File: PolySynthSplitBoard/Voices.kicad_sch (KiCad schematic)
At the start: 23 parts, among them U701 TCA9548APWR, U702 V1, U703 V4, U704 V2, U705 V5, U706 V3, U707 V6

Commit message: SPI and board tweaks
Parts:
- added R716: LOOP, Resistor_THT:R_Axial_DIN0204_L3.6mm_D1.6mm_P5.08mm_Horizontal, symbol Device:R_US
- added TP701: SCLV1, TestPoint:TestPoint_THTPad_D1.0mm_Drill0.5mm_VAL, symbol Connector:TestPoint
- added TP702: SDAV1, TestPoint:TestPoint_THTPad_D1.0mm_Drill0.5mm_VAL, symbol Connector:TestPoint
- added TP703: SCLV2, TestPoint:TestPoint_THTPad_D1.0mm_Drill0.5mm_VAL, symbol Connector:TestPoint
- added TP704: SDAV2, TestPoint:TestPoint_THTPad_D1.0mm_Drill0.5mm_VAL, symbol Connector:TestPoint
- added TP705: SCLV3, TestPoint:TestPoint_THTPad_D1.0mm_Drill0.5mm_VAL, symbol Connector:TestPoint
- added TP706: SDAV3, TestPoint:TestPoint_THTPad_D1.0mm_Drill0.5mm_VAL, symbol Connector:TestPoint
- added TP707: SCLV4, TestPoint:TestPoint_THTPad_D1.0mm_Drill0.5mm_VAL, symbol Connector:TestPoint
- added TP708: SDAV4, TestPoint:TestPoint_THTPad_D1.0mm_Drill0.5mm_VAL, symbol Connector:TestPoint
- added TP709: SCLV5, TestPoint:TestPoint_THTPad_D1.0mm_Drill0.5mm_VAL, symbol Connector:TestPoint
- added TP710: SDAV5, TestPoint:TestPoint_THTPad_D1.0mm_Drill0.5mm_VAL, symbol Connector:TestPoint
- added TP711: SCLV6, TestPoint:TestPoint_THTPad_D1.0mm_Drill0.5mm_VAL, symbol Connector:TestPoint
- added TP712: SDAV6, TestPoint:TestPoint_THTPad_D1.0mm_Drill0.5mm_VAL, symbol Connector:TestPoint
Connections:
- net GND: now also R716.1, R716.2
- net SCL_V1: now also TP701.1
- net SCL_V2: now also TP703.1
- net SCL_V3: now also TP705.1
- net SCL_V4: now also TP707.1
- net SCL_V5: now also TP709.1
- net SCL_V6: now also TP711.1
- net SDA_V1: now also TP702.1
- net SDA_V2: now also TP704.1
- net SDA_V3: now also TP706.1
- net SDA_V4: now also TP708.1
- net SDA_V5: now also TP710.1
- net SDA_V6: now also TP712.1

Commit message: mod matrix logic stuff
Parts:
- R701, R703, R704, R705, R706, R707, R708, R709, R710, R711, R712, R713, R714, R715: value 12k -> 4k7
- TP701: value SCLV1 -> TestPoint; now left out of the parts list
- TP702: value SDAV1 -> TestPoint; now left out of the parts list
- TP703: value SCLV2 -> TestPoint; now left out of the parts list
- TP704: value SDAV2 -> TestPoint; now left out of the parts list
- TP705: value SCLV3 -> TestPoint; now left out of the parts list
- TP706: value SDAV3 -> TestPoint; now left out of the parts list
- TP707: value SCLV4 -> TestPoint; now left out of the parts list
- TP708: value SDAV4 -> TestPoint; now left out of the parts list
- TP709: value SCLV5 -> TestPoint; now left out of the parts list
- TP710: value SDAV5 -> TestPoint; now left out of the parts list
- TP711: value SCLV6 -> TestPoint; now left out of the parts list
- TP712: value SDAV6 -> TestPoint; now left out of the parts list
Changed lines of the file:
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@@
 		(unit 1)
 		(exclude_from_sim no)
-		(in_bom yes)
+		(in_bom no)
 		(on_board yes)
 		(dnp no)
@@
 			)
 		)
-		(property "Value" "SDAV3"
+		(property "Value" "TestPoint"
 			(at 53.34 216.1539 0)
 			(effects
@@
 			)
 		)
-		(property "Value" "12k"
+		(property "Value" "4k7"
 			(at 66.802 112.268 0)
 			(effects
@@
 			)
 		)
-		(property "Value" "12k"
+		(property "Value" "4k7"
 			(at 311.658 145.923 0)
 			(effects
@@
 			)
 		)
-		(property "Value" "12k"
+		(property "Value" "4k7"
 			(at 55.88 112.268 0)
 			(effects
@@
 		(unit 1)
 		(exclude_from_sim no)
-		(in_bom yes)
+		(in_bom no)
 		(on_board yes)
 		(dnp no)
@@
 			)
 		)
-		(property "Value" "SCLV4"
+		(property "Value" "TestPoint"
 			(at 74.93 177.7999 0)
 			(effects
@@
 			)
 		)
-		(property "Value" "12k"
+		(property "Value" "4k7"
 			(at 320.294 145.923 0)
 			(effects
@@
 		(unit 1)
 		(exclude_from_sim no)
-		(in_bom yes)
+		(in_bom no)
 		(on_board yes)
 		(dnp no)
@@
 			)
 		)
-		(property "Value" "SCLV6"
+		(property "Value" "TestPoint"
 			(at 76.2 208.7879 0)
 			(effects
@@
 			)
 		)
-		(property "Value" "12k"
+		(property "Value" "4k7"
 			(at 172.974 146.431 0)
 			(effects
@@
 		(unit 1)
 		(exclude_from_sim no)
-		(in_bom yes)
+		(in_bom no)
 		(on_board yes)
 		(dnp no)
@@
 			)
 		)
-		(property "Value" "SCLV3"
+		(property "Value" "TestPoint"
 			(at 53.34 209.0419 0)
 			(effects
@@
 		(unit 1)
 		(exclude_from_sim no)
-		(in_bom yes)
+		(in_bom no)
 		(on_board yes)
 		(dnp no)
@@
 			)
 		)
-		(property "Value" "SCLV1"
+		(property "Value" "TestPoint"
 			(at 52.07 177.5459 0)
 			(effects
@@
 			)
 		)
-		(property "Value" "12k"
+		(property "Value" "4k7"
 			(at 170.815 84.963 0)
 			(effects
@@
 		(unit 1)
 		(exclude_from_sim no)
-		(in_bom yes)
+		(in_bom no)
 		(on_board yes)
 		(dnp no)
@@
 			)
 		)
-		(property "Value" "SDAV2"
+		(property "Value" "TestPoint"
 			(at 53.34 200.4059 0)
 			(effects
@@
 			)
 		)
-		(property "Value" "12k"
+		(property "Value" "4k7"
 			(at 243.205 146.177 0)
 			(effects
@@
 			)
 		)
-		(property "Value" "12k"
+		(property "Value" "4k7"
 			(at 318.135 84.455 0)
 			(effects
@@
 		(unit 1)
 		(exclude_from_sim no)
-		(in_bom yes)
+		(in_bom no)
 		(on_board yes)
 		(dnp no)
@@
 			)
 		)
-		(property "Value" "SDAV5"
+		(property "Value" "TestPoint"
 			(at 76.2 200.4059 0)
 			(effects
@@
 			)
 		)
-		(property "Value" "12k"
+		(property "Value" "4k7"
 			(at 309.499 84.455 0)
 			(effects
@@
 		(unit 1)
 		(exclude_from_sim no)
-		(in_bom yes)
+		(in_bom no)
 		(on_board yes)
 		(dnp no)
@@
 			)
 		)
-		(property "Value" "SCLV2"
+		(property "Value" "TestPoint"
 			(at 52.07 193.2939 0)
 			(effects
@@
 			)
 		)
-		(property "Value" "12k"
+		(property "Value" "4k7"
 			(at 249.682 84.709 0)
 			(effects
@@
 			)
 		)
-		(property "Value" "12k"
+		(property "Value" "4k7"
 			(at 241.046 84.709 0)
 			(effects
@@
 			)
 		)
-		(property "Value" "12k"
+		(property "Value" "4k7"
 			(at 181.61 146.431 0)
 			(effects
@@
 		(unit 1)
 		(exclude_from_sim no)
-		(in_bom yes)
+		(in_bom no)
 		(on_board yes)
 		(dnp no)
@@
 			)
 		)
-		(property "Value" "SDAV6"
+		(property "Value" "TestPoint"
 			(at 76.2 215.8999 0)
 			(effects
@@
 		(unit 1)
 		(exclude_from_sim no)
-		(in_bom yes)
+		(in_bom no)
 		(on_board yes)
 		(dnp no)
@@
 			)
 		)
-		(property "Value" "SDAV4"
+		(property "Value" "TestPoint"
 			(at 76.2 184.9119 0)
 			(effects
@@
 			)
 		)
-		(property "Value" "12k"
+		(property "Value" "4k7"
 			(at 179.451 84.963 0)
 			(effects
@@
 		(unit 1)
 		(exclude_from_sim no)
-		(in_bom yes)
+		(in_bom no)
 		(on_board yes)
 		(dnp no)
@@
 			)
 		)
-		(property "Value" "SDAV1"
+		(property "Value" "TestPoint"
 			(at 52.07 184.6579 0)
 			(effects
@@
 		(unit 1)
 		(exclude_from_sim no)
-		(in_bom yes)
+		(in_bom no)
 		(on_board yes)
 		(dnp no)
@@
 			)
 		)
-		(property "Value" "SCLV5"
+		(property "Value" "TestPoint"
 			(at 76.2 193.2939 0)
 			(effects
@@
 			)
 		)
-		(property "Value" "12k"
+		(property "Value" "4k7"
 			(at 251.841 146.177 0)
 			(effects

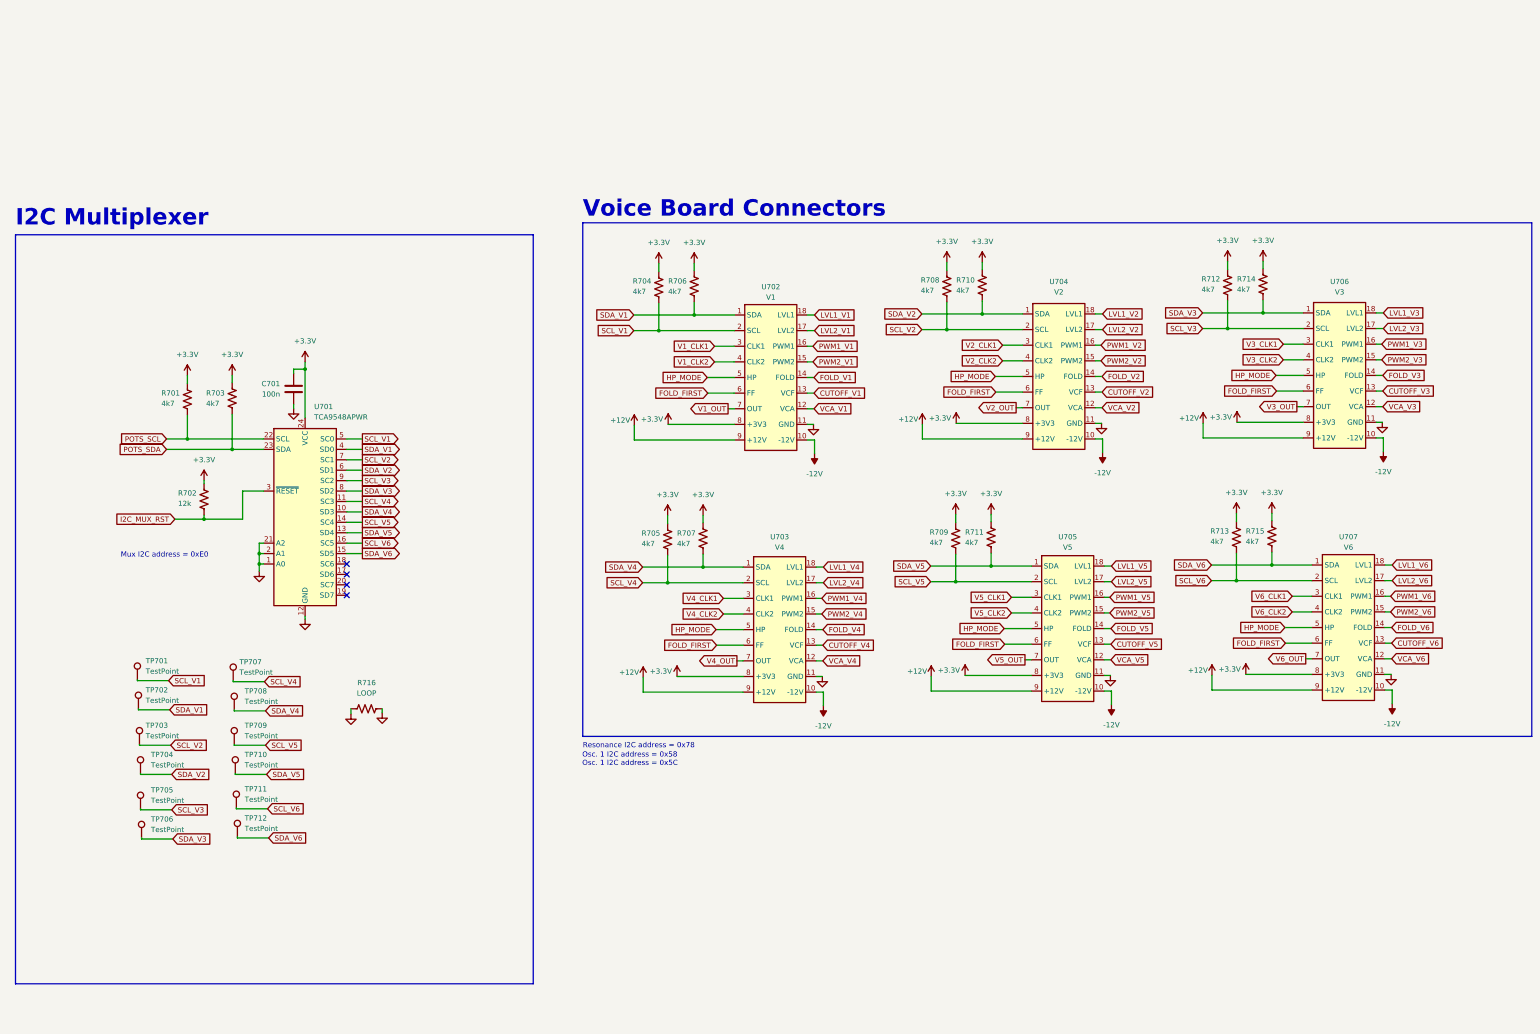
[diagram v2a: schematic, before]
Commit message: switching to 20p mezzanine connectors
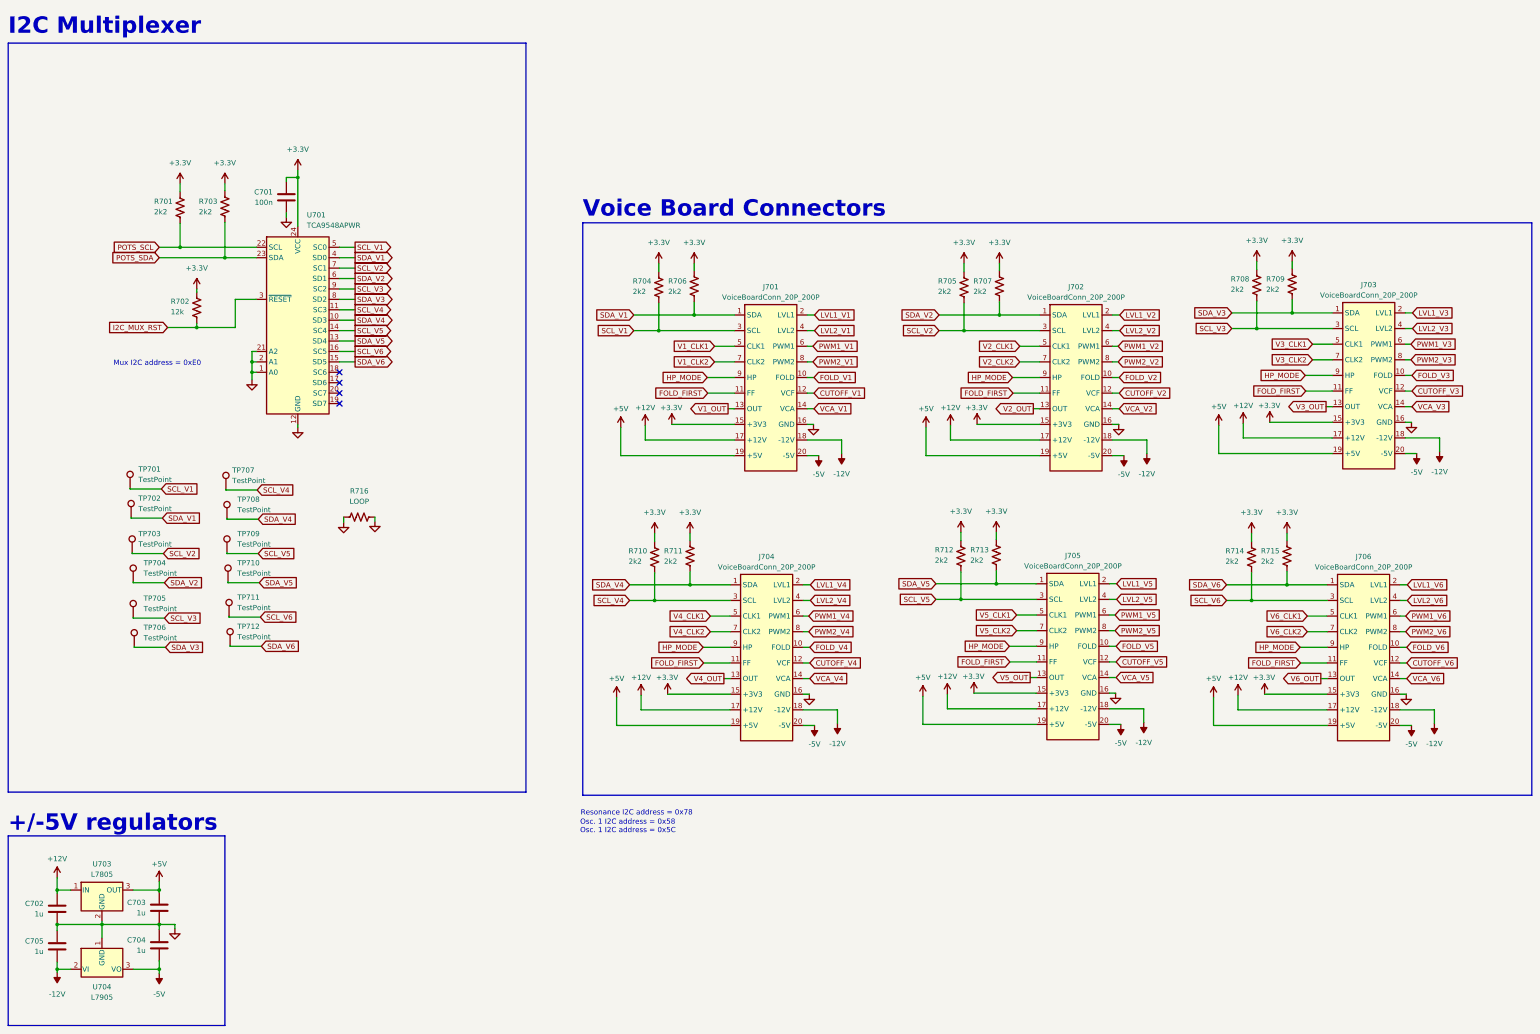
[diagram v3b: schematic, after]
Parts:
- removed U702: V1, Package_DIP:DIP-18_W7.62mm_Socket, symbol Connector_Audio:VoiceBoardConn_DIP18
- removed U703: V4, Package_DIP:DIP-18_W7.62mm_Socket, symbol Connector_Audio:VoiceBoardConn_DIP18
- removed U704: V2, Package_DIP:DIP-18_W7.62mm_Socket, symbol Connector_Audio:VoiceBoardConn_DIP18
- removed U705: V5, Package_DIP:DIP-18_W7.62mm_Socket, symbol Connector_Audio:VoiceBoardConn_DIP18
- removed U706: V3, Package_DIP:DIP-18_W7.62mm_Socket, symbol Connector_Audio:VoiceBoardConn_DIP18
- removed U707: V6, Package_DIP:DIP-18_W7.62mm_Socket, symbol Connector_Audio:VoiceBoardConn_DIP18
- added C702, C703, C704, C705: 1u, Capacitor_SMD:C_0805_2012Metric, symbol Device:C
- added J701, J702, J703, J704, J705, J706: VoiceBoardConn_20P_200P, Connector_PinHeader_2.00mm:PinHeader_2x10_P2.00mm_Vertical, symbol Connector_Audio:VoiceBoardConn_20P_200P
- added U703: L7805, Package_TO_SOT_THT:TO-220-3_Vertical, symbol Regulator_Linear:L7805
- added U704: L7905, Package_TO_SOT_THT:TO-220-3_Vertical, symbol Regulator_Linear:L7905
- R701, R703, R704, R705, R706, R707, R708, R709, R710, R711, R712, R713, R714, R715: value 4k7 -> 2k2
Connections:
- net +12V: now also C702.1, J701.17 (+12V), J702.17 (+12V), J703.17 (+12V), J704.17 (+12V), J705.17 (+12V), J706.17 (+12V), U703.1 (IN)
- net +3.3V: now also J701.15 (+3V3), J702.15 (+3V3), J703.15 (+3V3), J704.15 (+3V3), J705.15 (+3V3), J706.15 (+3V3)
- net -12V: now also C705.2, J701.18 (-12V), J702.18 (-12V), J703.18 (-12V), J704.18 (-12V), J705.18 (-12V), J706.18 (-12V), U704.2 (VI)
- net CUTOFF_V1: now also J701.12 (VCF)
- net CUTOFF_V2: now also J702.12 (VCF)
- net CUTOFF_V3: now also J703.12 (VCF)
- net CUTOFF_V4: now also J704.12 (VCF)
- net CUTOFF_V5: now also J705.12 (VCF)
- net CUTOFF_V6: now also J706.12 (VCF)
- net FOLD_FIRST: now also J701.11 (FF), J702.11 (FF), J703.11 (FF), J704.11 (FF), J705.11 (FF), J706.11 (FF)
- net FOLD_V1: now also J701.10 (FOLD)
- net FOLD_V2: now also J702.10 (FOLD)
- net FOLD_V3: now also J703.10 (FOLD)
- net FOLD_V4: now also J704.10 (FOLD)
- net FOLD_V5: now also J705.10 (FOLD)
- net FOLD_V6: now also J706.10 (FOLD)
- net GND: now also C702.2, C703.2, C704.1, C705.1, J701.16 (GND), J702.16 (GND), J703.16 (GND), J704.16 (GND), J705.16 (GND), J706.16 (GND), U703.2 (GND), U704.1 (GND)
- net HP_MODE: now also J701.9 (HP), J702.9 (HP), J703.9 (HP), J704.9 (HP), J705.9 (HP), J706.9 (HP)
- net LVL1_V1: now also J701.2 (LVL1)
- net LVL1_V2: now also J702.2 (LVL1)
- net LVL1_V3: now also J703.2 (LVL1)
- net LVL1_V4: now also J704.2 (LVL1)
- net LVL1_V5: now also J705.2 (LVL1)
- net LVL1_V6: now also J706.2 (LVL1)
- net LVL2_V1: now also J701.4 (LVL2)
- net LVL2_V2: now also J702.4 (LVL2)
- net LVL2_V3: now also J703.4 (LVL2)
- net LVL2_V4: now also J704.4 (LVL2)
- net LVL2_V5: now also J705.4 (LVL2)
- net LVL2_V6: now also J706.4 (LVL2)
- net PWM1_V1: now also J701.6 (PWM1)
- net PWM1_V2: now also J702.6 (PWM1)
- net PWM1_V3: now also J703.6 (PWM1)
- net PWM1_V4: now also J704.6 (PWM1)
- net PWM1_V5: now also J705.6 (PWM1)
- net PWM1_V6: now also J706.6 (PWM1)
- net PWM2_V1: now also J701.8 (PWM2)
- net PWM2_V2: now also J702.8 (PWM2)
- net PWM2_V3: now also J703.8 (PWM2)
- net PWM2_V4: now also J704.8 (PWM2)
- net PWM2_V5: now also J705.8 (PWM2)
- net PWM2_V6: now also J706.8 (PWM2)
- net SCL_V1: now also J701.3 (SCL)
- net SCL_V2: now also R705.2, J702.3 (SCL); no longer R708.2
- net SCL_V3: now also R708.2, J703.3 (SCL); no longer R712.2
- net SCL_V4: now also R710.2, J704.3 (SCL); no longer R705.2
- net SCL_V5: now also R712.2, J705.3 (SCL); no longer R709.2
- net SCL_V6: now also R714.2, J706.3 (SCL); no longer R713.2
- net SDA_V1: now also J701.1 (SDA)
- net SDA_V2: now also R707.2, J702.1 (SDA); no longer R710.2
- net SDA_V3: now also R709.2, J703.1 (SDA); no longer R714.2
- net SDA_V4: now also R711.2, J704.1 (SDA); no longer R707.2
- net SDA_V5: now also R713.2, J705.1 (SDA); no longer R711.2
- net SDA_V6: now also J706.1 (SDA)
- net V1_CLK1: now also J701.5 (CLK1)
- net V1_CLK2: now also J701.7 (CLK2)
- net V1_OUT: now also J701.13 (OUT)
- net V2_CLK1: now also J702.5 (CLK1)
- net V2_CLK2: now also J702.7 (CLK2)
- net V2_OUT: now also J702.13 (OUT)
- net V3_CLK1: now also J703.5 (CLK1)
- net V3_CLK2: now also J703.7 (CLK2)
- net V3_OUT: now also J703.13 (OUT)
- net V4_CLK1: now also J704.5 (CLK1)
- net V4_CLK2: now also J704.7 (CLK2)
- net V4_OUT: now also J704.13 (OUT)
- net V5_CLK1: now also J705.5 (CLK1)
- net V5_CLK2: now also J705.7 (CLK2)
- net V5_OUT: now also J705.13 (OUT)
- net V6_CLK1: now also J706.5 (CLK1)
- net V6_CLK2: now also J706.7 (CLK2)
- net V6_OUT: now also J706.13 (OUT)
- net VCA_V1: now also J701.14 (VCA)
- net VCA_V2: now also J702.14 (VCA)
- net VCA_V3: now also J703.14 (VCA)
- net VCA_V4: now also J704.14 (VCA)
- net VCA_V5: now also J705.14 (VCA)
- net VCA_V6: now also J706.14 (VCA)
- new net +5V: C703.1, J701.19 (+5V), J702.19 (+5V), J703.19 (+5V), J704.19 (+5V), J705.19 (+5V), J706.19 (+5V), U703.3 (OUT)
- new net -5V: C704.2, J701.20 (-5V), J702.20 (-5V), J703.20 (-5V), J704.20 (-5V), J705.20 (-5V), J706.20 (-5V), U704.3 (VO)
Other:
- note added: "+/-5V regulators"
- moved on the sheet: C701, R701, R702, R703, R716, TP701, TP702, TP703, TP704, TP705, TP706, TP707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

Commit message: motherboard rev2 passing DRC
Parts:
- TP701: value TestPoint -> SCL_V1
- TP702: value TestPoint -> SDA_V1
- TP703: value TestPoint -> SCL_V2
- TP704: value TestPoint -> SDA_V2
- TP705: value TestPoint -> SCL_V3
- TP706: value TestPoint -> SDA_V3
- TP707: value TestPoint -> SCL_V4
- TP708: value TestPoint -> SDA_V4
- TP709: value TestPoint -> SCL_V5
- TP710: value TestPoint -> SDA_V5
- TP711: value TestPoint -> SCL_V6
- TP712: value TestPoint -> SDA_V6
